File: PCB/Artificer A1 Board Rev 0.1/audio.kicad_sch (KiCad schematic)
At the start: 17 parts, among them CN2 PJ-327A0-SMT

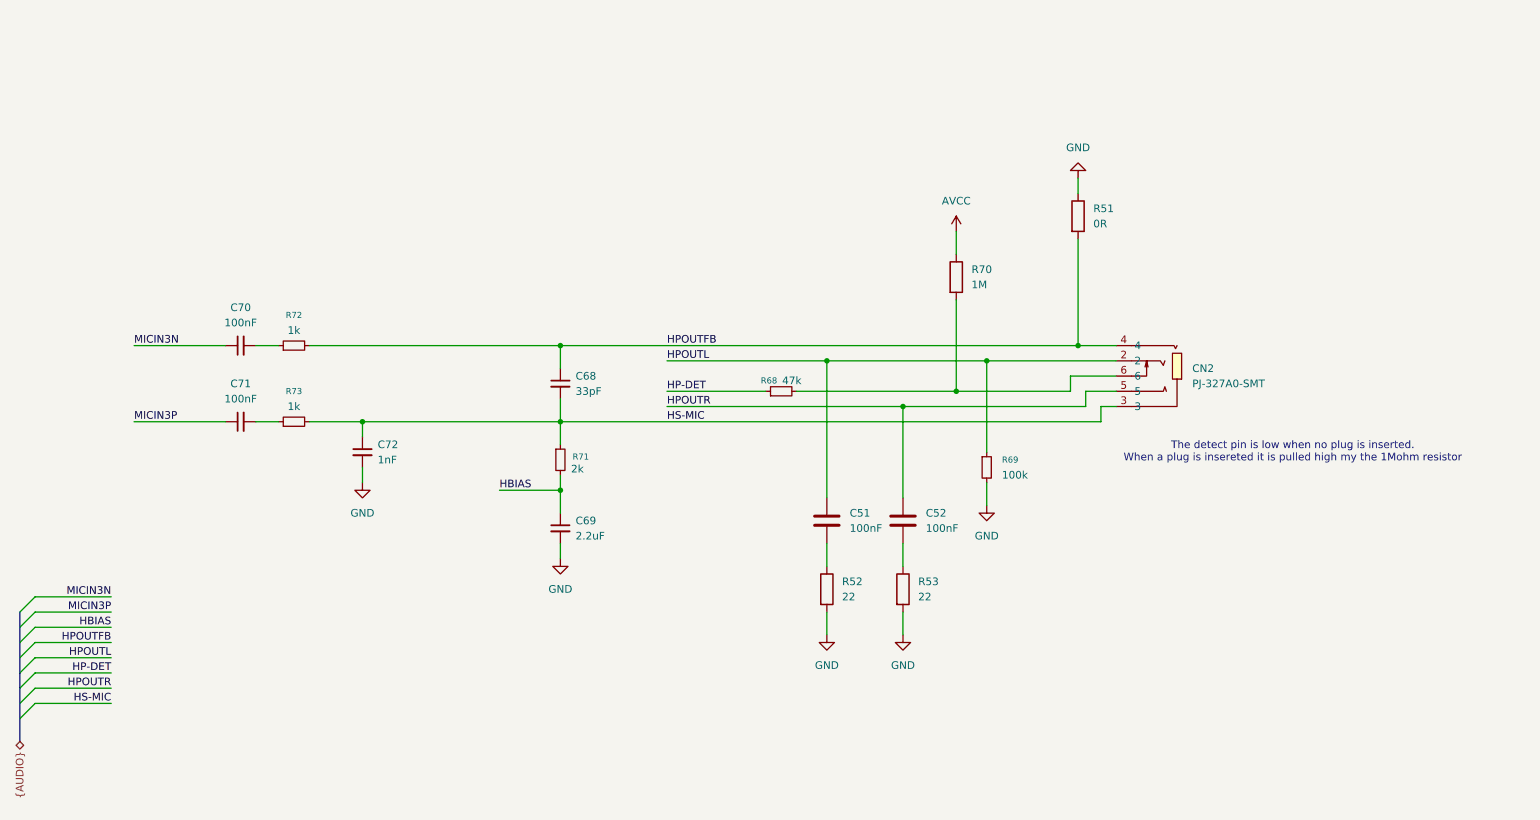
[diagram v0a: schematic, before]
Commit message: cleaned up, kicad 10 & usb c pd
migrated to Kicad 10,
added USB PD for power input
added capacitors inductors and resistor footprints
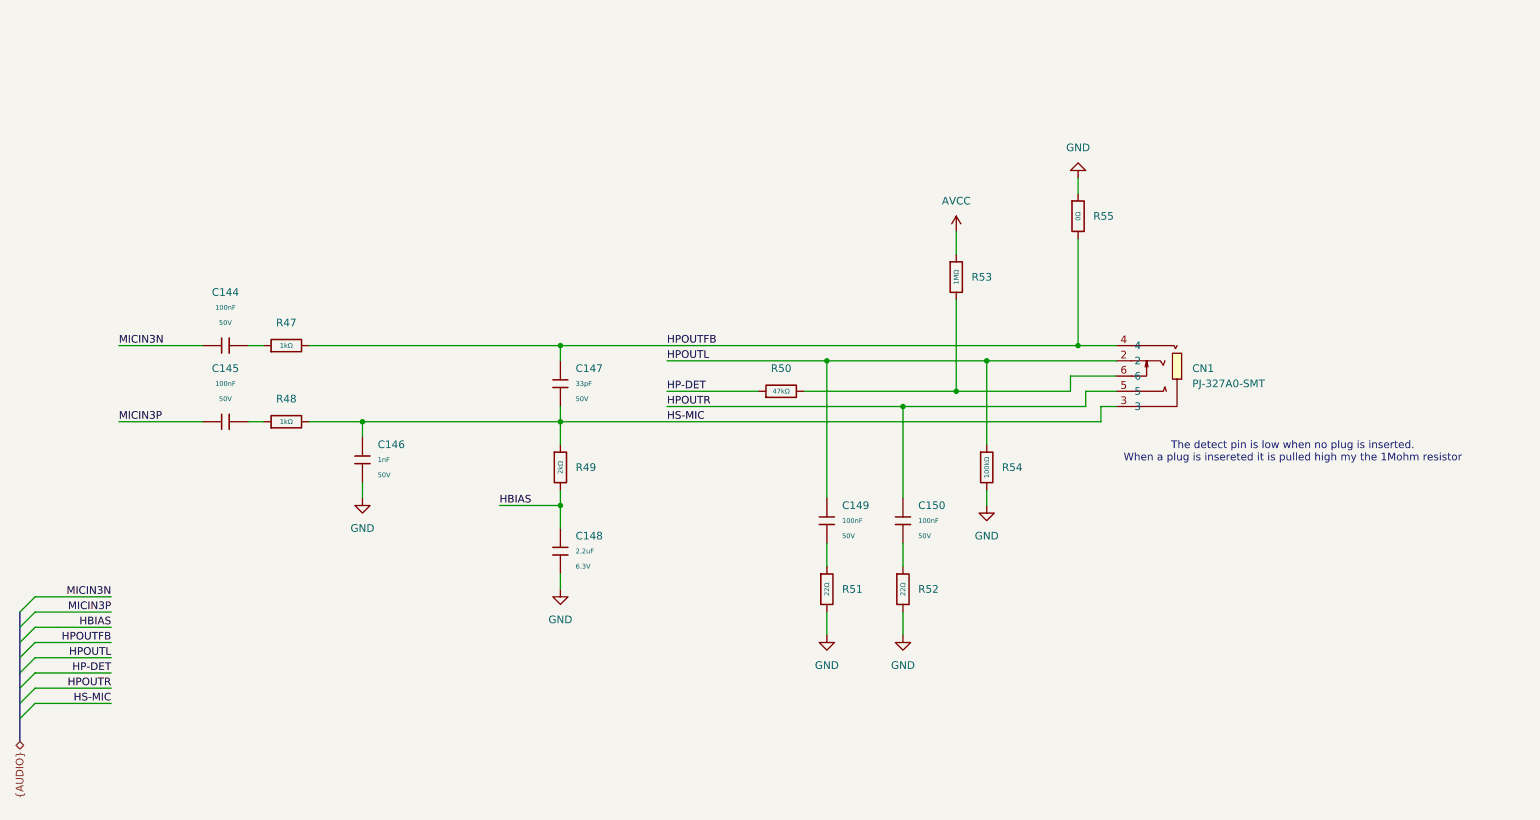
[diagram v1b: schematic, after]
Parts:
- removed C51, C52: 100nF, symbol Device:C
- removed C68: 33pF, symbol Device:C_Small
- removed C69: 2.2uF, symbol Device:C_Small
- removed C70, C71: 100nF, symbol Device:C_Small
- removed C72: 1nF, symbol Device:C_Small
- removed R51: 0R, symbol Device:R
- removed R52, R53: 22, symbol Device:R
- removed R68: 47k, symbol Device:R_Small
- removed R69: 100k, symbol Device:R_Small
- removed R70: 1M, symbol Device:R
- removed R71: 2k, symbol Device:R_Small
- removed R72, R73: 1k, symbol Device:R_Small
- added C144, C145, C149, C150: 100nF, PCM_JLCPCB:C_0402, symbol PCM_JLCPCB-Capacitors:0402,100nF,(2)
- added C146: 1nF, PCM_JLCPCB:C_0402, symbol PCM_JLCPCB-Capacitors:0402,1nF
- added C147: 33pF, PCM_JLCPCB:C_0402, symbol PCM_JLCPCB-Capacitors:0402,33pF
- added C148: 2.2uF, PCM_JLCPCB:C_0402, symbol PCM_JLCPCB-Capacitors:0402,2.2uF
- added R47, R48: 1kΩ, PCM_JLCPCB:R_0402, symbol PCM_JLCPCB-Resistors:0402,1kΩ
- added R49: 2kΩ, PCM_JLCPCB:R_0402, symbol PCM_JLCPCB-Resistors:0402,2kΩ
- added R50: 47kΩ, PCM_JLCPCB:R_0402, symbol PCM_JLCPCB-Resistors:0402,47kΩ
- added R51, R52: 22Ω, PCM_JLCPCB:R_0402, symbol PCM_JLCPCB-Resistors:0402,22Ω
- added R53: 1MΩ, PCM_JLCPCB:R_0402, symbol PCM_JLCPCB-Resistors:0402,1MΩ
- added R54: 100kΩ, PCM_JLCPCB:R_0402, symbol PCM_JLCPCB-Resistors:0402,100kΩ
- added R55: 0Ω, PCM_JLCPCB:R_0402, symbol PCM_JLCPCB-Resistors:0402,0Ω
- renumbered CN2 to CN1
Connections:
- net AVCC: now also R53.1
- net GND: now also C146.2, C148.2, R51.2, R52.2, R54.2, R55.1
- net HBIAS: now also C148.1, R49.2
- net HP-DET: now also R50.1
- net HPOUTFB: now also C147.1, R47.2, R55.2
- net HPOUTL: now also C149.2, R54.1
- net HPOUTR: now also C150.2
- net HS-MIC: now also C146.1, C147.2, R48.2, R49.1
- net MICIN3N: now also C144.1
- net MICIN3P: now also C145.1
- net at CN1.6: now also R50.2, R53.2
- new net: C144.2, R47.1
- new net: C149.1, R51.1
- new net: C145.2, R48.1
- new net: C150.1, R52.1

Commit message: worked on power pours
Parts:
- removed C144, C145, C149, C150: 100nF, PCM_JLCPCB:C_0402, symbol PCM_JLCPCB-Capacitors:0402,100nF,(2)
- removed C146: 1nF, PCM_JLCPCB:C_0402, symbol PCM_JLCPCB-Capacitors:0402,1nF
- removed C147: 33pF, PCM_JLCPCB:C_0402, symbol PCM_JLCPCB-Capacitors:0402,33pF
- removed C148: 2.2uF, PCM_JLCPCB:C_0402, symbol PCM_JLCPCB-Capacitors:0402,2.2uF
- removed R47, R48: 1kΩ, PCM_JLCPCB:R_0402, symbol PCM_JLCPCB-Resistors:0402,1kΩ
- removed R49: 2kΩ, PCM_JLCPCB:R_0402, symbol PCM_JLCPCB-Resistors:0402,2kΩ
- removed R50: 47kΩ, PCM_JLCPCB:R_0402, symbol PCM_JLCPCB-Resistors:0402,47kΩ
- removed R51, R52: 22Ω, PCM_JLCPCB:R_0402, symbol PCM_JLCPCB-Resistors:0402,22Ω
- removed R53: 1MΩ, PCM_JLCPCB:R_0402, symbol PCM_JLCPCB-Resistors:0402,1MΩ
- removed R54: 100kΩ, PCM_JLCPCB:R_0402, symbol PCM_JLCPCB-Resistors:0402,100kΩ
- removed R55: 0Ω, PCM_JLCPCB:R_0402, symbol PCM_JLCPCB-Resistors:0402,0Ω
- added C174, C175, C199, C200: 100nF, Capacitor_SMD:C_0201_0603Metric, symbol Cap:JLCPCB_Lib_Blank_Cap
- added C198, C202: 33pF, Capacitor_SMD:C_0201_0603Metric, symbol Cap:JLCPCB_Lib_Blank_Cap
- added C201: 1nF, Capacitor_SMD:C_0201_0603Metric, symbol Cap:JLCPCB_Lib_Blank_Cap
- added C353: 2.2uF, Capacitor_SMD:C_0201_0603Metric, symbol Cap:JLCPCB_Lib_Blank_Cap
- added CN3: PJ-393-8P_C49284725, easyeda:AUDIO-TH_PJ-393-8P, symbol easyeda:PJ-393-8P_C49284725
- added R233, R234: 1k, Resistor_SMD:R_0201_0603Metric, symbol Cap:JLCPCB_Res_Custom
- added R235: 2k, Resistor_SMD:R_0201_0603Metric, symbol Cap:JLCPCB_Res_Custom
- added R236: 47k, Resistor_SMD:R_0201_0603Metric, symbol Cap:JLCPCB_Res_Custom
- added R237: 0Ω, Resistor_SMD:R_0201_0603Metric, symbol Cap:JLCPCB_Res_Custom
- added R238, R239: 22Ω, Resistor_SMD:R_0201_0603Metric, symbol Cap:JLCPCB_Res_Custom
- added R240: 100k, Resistor_SMD:R_0201_0603Metric, symbol Cap:JLCPCB_Res_Custom
- CN1: now not fitted; now left out of the parts list
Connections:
- net AVCC: now also R240.1
- net GND: now also C201.1, C202.1, C353.1, R237.2, R238.2, R239.2
- net HBIAS: now also C353.2, R235.1
- net HP-DET: now also R236.2
- net HPOUTFB: now also C198.1, C202.2, CN3.4, R234.1, R237.1; no longer CN1.4
- net HPOUTL: now also C174.2, CN3.6; no longer CN1.2
- net HPOUTR: now also C175.2, CN3.3; no longer CN1.5
- net HS-MIC: now also C198.2, C201.2, CN3.1, R233.1, R235.2; no longer CN1.3
- net MICIN3N: now also C199.2
- net MICIN3P: now also C200.2
- new net: CN3.8, R236.1, R240.2
- new net: C174.1, R238.1
- new net: C175.1, R239.1
- new net: C200.1, R234.2
- new net: C199.1, R233.2
- no-connect marks 0 -> 3

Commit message: added fan and PD debugging circuitry
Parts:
- R240: value 100k -> 1M
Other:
- note added: "Close to Headphone Jack"
- note added: "Close to Headphone Jack for ESD"
- note added: "Close to Headphone Jack for hp ground"
- note added: "Close to SoC"
- note added: "Close to jack"
- note added: "Place bias network close to SoC"
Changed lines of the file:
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@@
 		(company "Matthew Spotten")
+	)
+	(text "Close to jack"
+		(exclude_from_sim no)
+		(at 174.498 64.008 0)
+		(effects
+			(font
+				(size 1.27 1.27)
+			)
+			(justify left)
+		)
+	)
+	(text "Close to Headphone\nJack"
+		(exclude_from_sim no)
+		(at 156.972 119.888 0)
+		(effects
+			(font
+				(size 1.27 1.27)
+			)
+			(justify right)
+		)
+	)
+	(text "Place bias network\nclose to SoC"
+		(exclude_from_sim no)
+		(at 74.168 77.724 0)
+		(effects
+			(font
+				(size 1.27 1.27)
+			)
+			(justify left)
+		)
+	)
+	(text "Close to Headphone\nJack for ESD"
+		(exclude_from_sim no)
+		(at 104.14 111.76 0)
+		(effects
+			(font
+				(size 1.27 1.27)
+			)
+			(justify left)
+		)
+	)
+	(text "Close to SoC"
+		(exclude_from_sim no)
+		(at 146.558 71.628 0)
+		(effects
+			(font
+				(size 1.27 1.27)
+			)
+			(justify left)
+		)
+	)
+	(text "Close to Headphone\nJack for hp ground"
+		(exclude_from_sim no)
+		(at 209.55 126.492 0)
+		(effects
+			(font
+				(size 1.27 1.27)
+			)
+			(justify left)
+		)
 	)
 	(text "The detect pin is low when no plug is inserted.\nWhen a plug is insereted it is pulled high my the 1Mohm resistor"
@@
 			)
 			(justify right)
+		)
+	)
+	(rule_area
+		(exclude_from_sim no)
+		(in_bom yes)
+		(on_board yes)
+		(dnp no)
+		(polyline
+			(pts
+				(xy 144.78 68.58) (xy 162.56 68.58) (xy 162.56 105.41) (xy 144.78 105.41)
+			)
+			(stroke
+				(width 0)
+				(type dash)
+			)
+			(fill
+				(type none)
+			)
+		)
+	)
+	(rule_area
+		(exclude_from_sim no)
+		(in_bom yes)
+		(on_board yes)
+		(dnp no)
+		(polyline
+			(pts
+				(xy 55.88 58.42) (xy 133.35 58.42) (xy 133.35 102.87) (xy 82.55 102.87) (xy 82.55 123.19) (xy 55.88 123.19)
+				(xy 55.88 59.69)
+			)
+			(stroke
+				(width 0)
+				(type dash)
+			)
+			(fill
+				(type none)
+			)
+		)
+	)
+	(rule_area
+		(exclude_from_sim no)
+		(in_bom yes)
+		(on_board yes)
+		(dnp no)
+		(polyline
+			(pts
+				(xy 198.12 116.84) (xy 233.68 116.84) (xy 233.68 132.08) (xy 198.12 132.08)
+			)
+			(stroke
+				(width 0)
+				(type dash)
+			)
+			(fill
+				(type none)
+			)
+		)
+	)
+	(rule_area
+		(exclude_from_sim no)
+		(in_bom yes)
+		(on_board yes)
+		(dnp no)
+		(polyline
+			(pts
+				(xy 172.72 60.96) (xy 190.5 60.96) (xy 190.5 97.79) (xy 172.72 97.79)
+			)
+			(stroke
+				(width 0)
+				(type dash)
+			)
+			(fill
+				(type none)
+			)
+		)
+	)
+	(rule_area
+		(exclude_from_sim no)
+		(in_bom yes)
+		(on_board yes)
+		(dnp no)
+		(polyline
+			(pts
+				(xy 93.98 105.41) (xy 127 105.41) (xy 127 120.65) (xy 93.98 120.65)
+			)
+			(stroke
+				(width 0)
+				(type dash)
+			)
+			(fill
+				(type none)
+			)
+		)
+	)
+	(rule_area
+		(exclude_from_sim no)
+		(in_bom yes)
+		(on_board yes)
+		(dnp no)
+		(polyline
+			(pts
+				(xy 134.62 110.49) (xy 185.42 110.49) (xy 185.42 138.43) (xy 134.62 138.43)
+			)
+			(stroke
+				(width 0)
+				(type dash)
+			)
+			(fill
+				(type none)
+			)
 		)
 	)
@@
 			)
 		)
-		(property "Value" "100k"
+		(property "Value" "1M"
 			(at 182.88 80.01 90)
 			(show_name no)
